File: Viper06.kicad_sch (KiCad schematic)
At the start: 0 parts

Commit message: Finish schematics and layout
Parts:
- added C0: 220p, Capacitor_SMD:C_0603_1608Metric, symbol Device:C
- added C1: 4.7u, Capacitor_THT:CP_Radial_D8.0mm_P3.50mm, symbol Device:C_Polarized_US
- added C2: 10u, Capacitor_THT:CP_Radial_D10.0mm_P5.00mm, symbol Device:C_Polarized_US
- added C3: 1u, Capacitor_SMD:C_1206_3216Metric, symbol Device:C
- added C4, C8: 0.1u, Capacitor_SMD:C_0805_2012Metric, symbol Device:C
- added C6: 47u, Capacitor_THT:CP_Radial_D6.3mm_P2.50mm, symbol Device:C_Polarized_US
- added C9: 2.2n, Capacitor_SMD:C_0603_1608Metric, symbol Device:C
- added D1, D2: D, Components:DIOM5127X229N, symbol Device:D
- added D5: D, Components:DIOM5126X265N, symbol Device:D
- added D8: D, Diode_SMD:D_SMA, symbol Device:D
- added IC1: VIPER06LS, Components:SOP100P600X175-10N, symbol VIPER06LS:VIPER06LS
- added J1, J2: Screw_Terminal_01x02, TerminalBlock_Phoenix:TerminalBlock_Phoenix_PT-1,5-2-3.5-H_1x02_P3.50mm_Horizontal, symbol Connector:Screw_Terminal_01x02
- added L0: 470uH, Inductor_THT:L_Axial_L13.0mm_D4.5mm_P5.08mm_Vertical_Fastron_HCCC, symbol Device:L
- added L1: 1mH, Inductor_THT:L_Radial_D7.8mm_P5.00mm_Fastron_07HCP, symbol Device:L
- added R0: 6.8, Resistor_THT:R_Axial_DIN0207_L6.3mm_D2.5mm_P10.16mm_Horizontal, symbol Device:R
- added R1: 1k, Resistor_SMD:R_0805_2012Metric, symbol Device:R
- added R2: 10.6k, Resistor_SMD:R_0805_2012Metric, symbol Device:R
- added R3: R3, Resistor_THT:R_Axial_DIN0207_L6.3mm_D2.5mm_P10.16mm_Horizontal, symbol Device:R
- added R4: 29.4k, Resistor_SMD:R_0805_2012Metric, symbol Device:R
- added R5: 10k, Resistor_SMD:R_0805_2012Metric, symbol Device:R
- added Rdz1: 47k, Resistor_SMD:R_0805_2012Metric, symbol Device:R
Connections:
- new net: J1.2 (Pin_2), R0.1
- new net: C3.1, D2.1 (K), IC1.2 (VDD)
- new net: C0.2, C3.2, C4.2, C8.1, C9.1, D5.1 (K), IC1.1 (GND), L1.1, R2.2, R3.1
- new net: C9.2, IC1.5 (COMP), R5.2
- new net: C0.1, IC1.4 (FB), R2.1, R4.2
- new net: C8.2, R5.1
- new net: D1.2 (A), R0.2
- new net: C4.1, D8.1 (K), R4.1
- new net: C1.1, D1.1 (K), L0.1, R1.1
- new net: IC1.3 (LIM), R3.2
- new net 12V: C6.1, D2.2 (A), D8.2 (A), J2.1 (Pin_1), L1.2, Rdz1.1
- new net DRAIN: C2.1, IC1.10 (DRAIN_5), IC1.6 (DRAIN_1), IC1.7 (DRAIN_2), IC1.8 (DRAIN_3), IC1.9 (DRAIN_4), L0.2, R1.2
- new net GND: C1.2, C2.2, C6.2, D5.2 (A), J1.1 (Pin_1), J2.2 (Pin_2), Rdz1.2

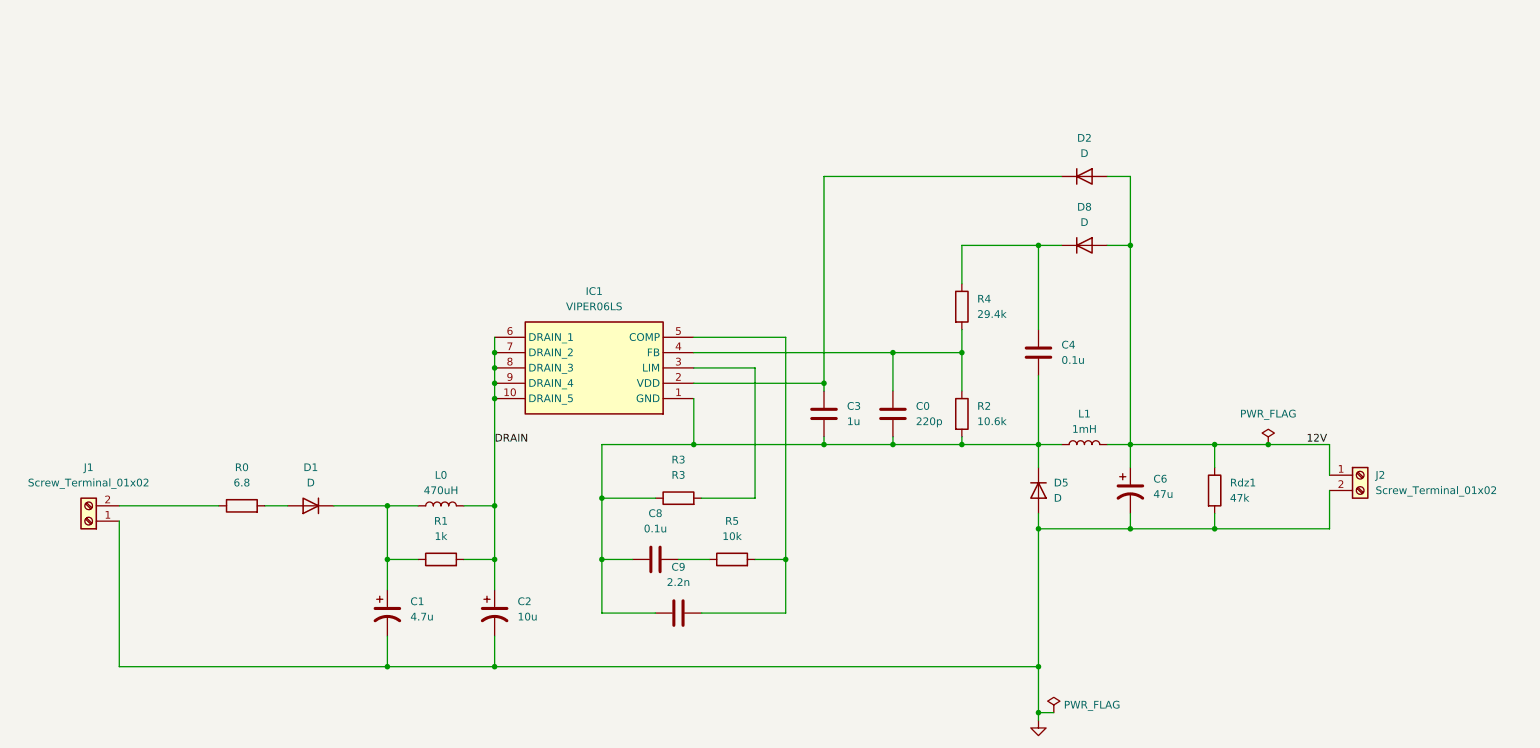
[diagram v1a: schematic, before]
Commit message: Add comments to schematics
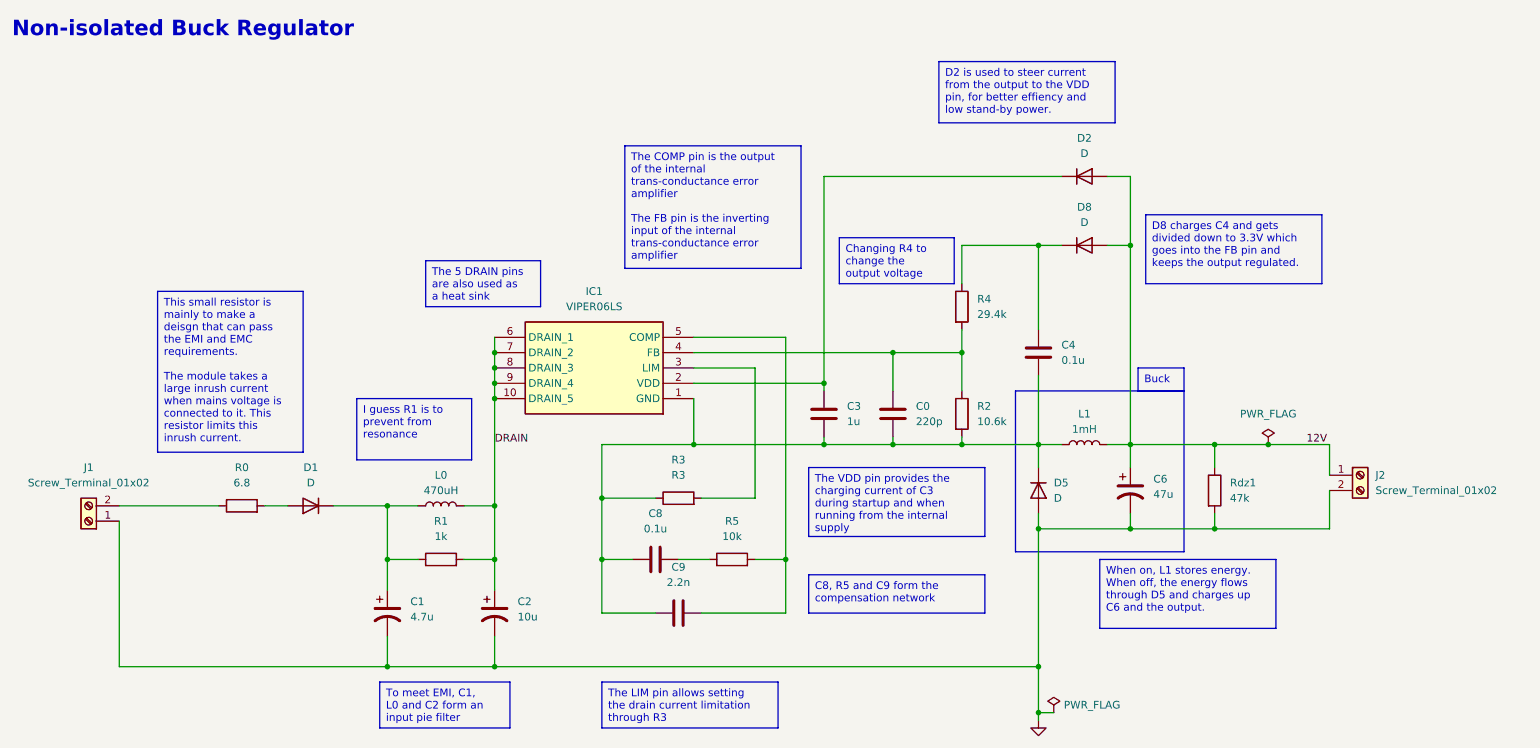
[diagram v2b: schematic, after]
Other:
- note added: "Non-isolated Buck Regulator"
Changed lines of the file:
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@@
     (stroke (width 0) (type default))
+  )
+  (rectangle (start 190.5 87.63) (end 218.44 114.3)
+    (stroke (width 0) (type default))
+    (fill (type none))
+  )
+  (text_box "Buck"
+    (at 210.82 83.82 0) (size 7.62 3.81)
+    (stroke (width 0) (type default))
+    (fill (type none))
+    (effects (font (size 1.27 1.27)) (justify left top))
+  )
+  (text_box "I guess R1 is to prevent from resonance"
+    (at 81.28 88.9 0) (size 19.05 10.16)
+    (stroke (width 0) (type default))
+    (fill (type none))
+    (effects (font (size 1.27 1.27)) (justify left top))
+  )
+  (text_box "The 5 DRAIN pins are also used as a heat sink"
+    (at 92.71 66.04 0) (size 19.05 7.62)
+    (stroke (width 0) (type default))
+    (fill (type none))
+    (effects (font (size 1.27 1.27)) (justify left top))
+  )
+  (text_box "The VDD pin provides the charging current of C3 during startup and when running from the internal supply"
+    (at 156.21 100.33 0) (size 29.21 11.43)
+    (stroke (width 0) (type default))
+    (fill (type none))
+    (effects (font (size 1.27 1.27)) (justify left top))
+  )
+  (text_box "When on, L1 stores energy. When off, the energy flows through D5 and charges up C6 and the output."
+    (at 204.47 115.57 0) (size 29.21 11.43)
+    (stroke (width 0) (type default))
+    (fill (type none))
+    (effects (font (size 1.27 1.27)) (justify left top))
+  )
+  (text_box "The LIM pin allows setting the drain current limitation through R3"
+    (at 121.92 135.89 0) (size 29.21 7.62)
+    (stroke (width 0) (type default))
+    (fill (type none))
+    (effects (font (size 1.27 1.27)) (justify left top))
+  )
+  (text_box "D2 is used to steer current from the output to the VDD pin, for better effiency and low stand-by power."
+    (at 177.8 33.02 0) (size 29.21 10.16)
+    (stroke (width 0) (type default))
+    (fill (type none))
+    (effects (font (size 1.27 1.27)) (justify left top))
+  )
+  (text_box "This small resistor is mainly to make a deisgn that can pass the EMI and EMC requirements.\n\nThe module takes a large inrush current when mains voltage is connected to it. This resistor limits this inrush current."
+    (at 48.26 71.12 0) (size 24.13 26.67)
+    (stroke (width 0) (type default))
+    (fill (type none))
+    (effects (font (size 1.27 1.27)) (justify left top))
+  )
+  (text_box "The COMP pin is the output of the internal trans-conductance error amplifier\n\nThe FB pin is the inverting input of the internal trans-conductance error amplifier"
+    (at 125.73 46.99 0) (size 29.21 20.32)
+    (stroke (width 0) (type default))
+    (fill (type none))
+    (effects (font (size 1.27 1.27)) (justify left top))
+  )
+  (text_box "C8, R5 and C9 form the compensation network"
+    (at 156.21 118.11 0) (size 29.21 6.35)
+    (stroke (width 0) (type default))
+    (fill (type none))
+    (effects (font (size 1.27 1.27)) (justify left top))
+  )
+  (text_box "D8 charges C4 and gets divided down to 3.3V which goes into the FB pin and keeps the output regulated."
+    (at 212.09 58.42 0) (size 29.21 11.43)
+    (stroke (width 0) (type default))
+    (fill (type none))
+    (effects (font (size 1.27 1.27)) (justify left top))
+  )
+  (text_box "To meet EMI, C1, L0 and C2 form an input pie filter"
+    (at 85.09 135.89 0) (size 21.59 7.62)
+    (stroke (width 0) (type default))
+    (fill (type none))
+    (effects (font (size 1.27 1.27)) (justify left top))
+  )
+  (text_box "Changing R4 to change the output voltage"
+    (at 161.29 62.23 0) (size 19.05 7.62)
+    (stroke (width 0) (type default))
+    (fill (type none))
+    (effects (font (size 1.27 1.27)) (justify left top))
+  )
+  (text "Non-isolated Buck Regulator" (at 24.13 29.21 0)
+    (effects (font (size 2.56 2.56) (thickness 0.512) bold) (justify left bottom))
   )
   (label "12V" (at 238.76 96.52 0) (fields_autoplaced)
